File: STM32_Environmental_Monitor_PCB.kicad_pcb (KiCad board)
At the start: 2 copper layers, 90 x 81 mm, 29 parts, among them Q1 Q_NPN_EBC, Q2 Q_NPN_EBC, Q3 Q_NPN_EBC, Q4 Q_NPN_EBC, SW1 SW_Push, U1 NUCLEO-F303K8, U2 BME280-Module, U3 CC56-12SURKWA, U4 74HC595, U5 74HC595

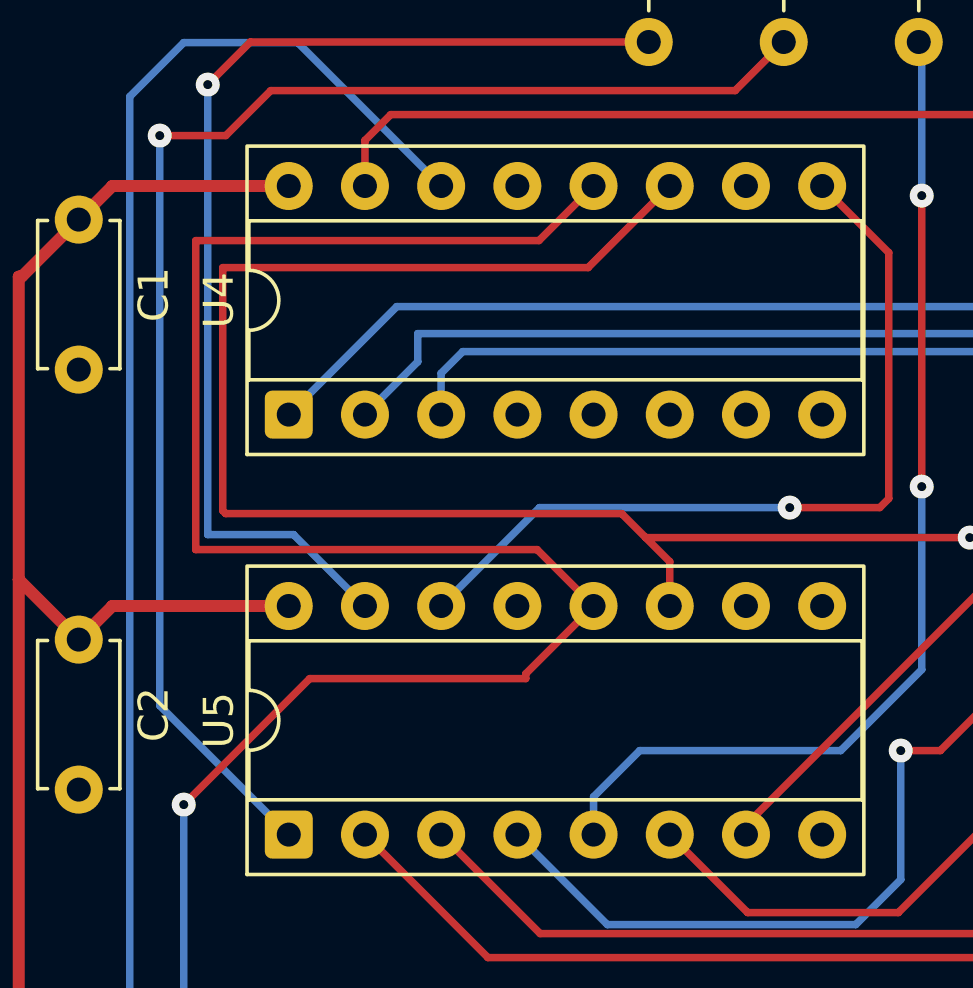
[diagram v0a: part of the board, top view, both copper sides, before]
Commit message: Fix 74HC595 control pins and update PCB fabrication files
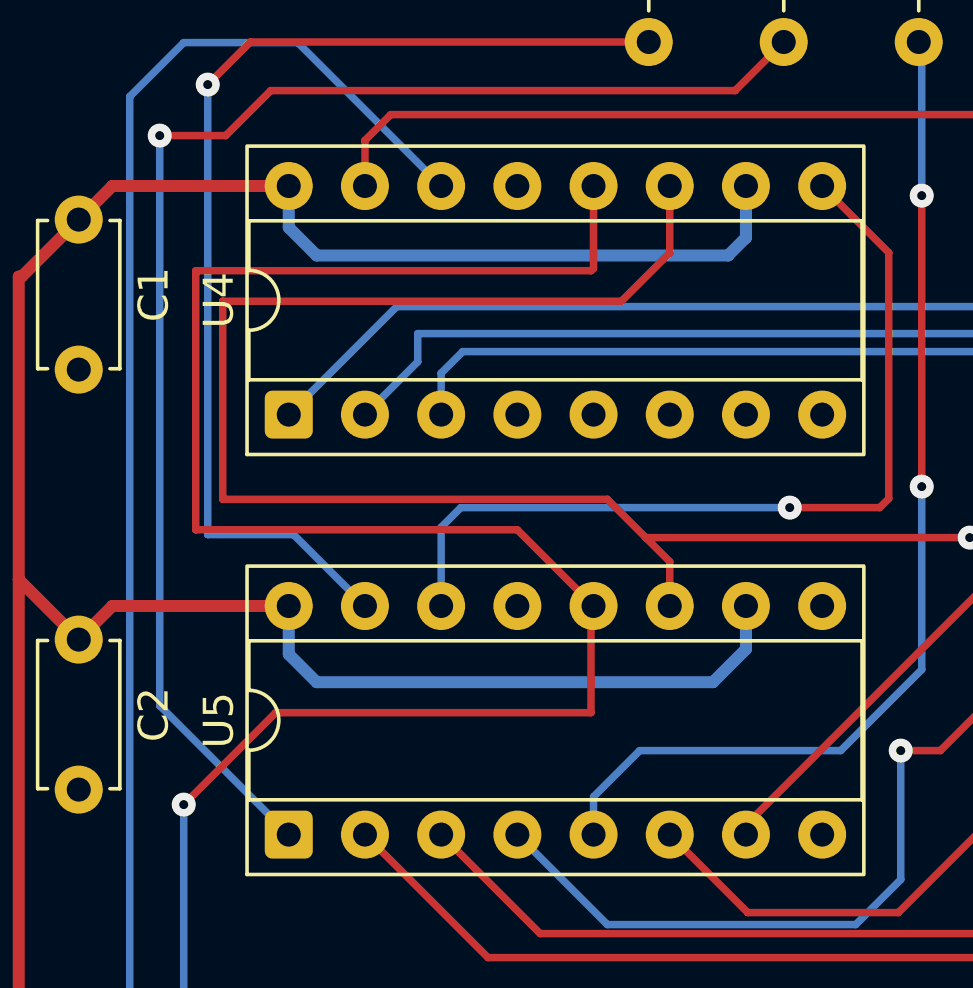
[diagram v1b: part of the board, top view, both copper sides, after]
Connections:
- U4 pad 10: unconnected-(U4-~{SRCLR}-Pad10) -> +3.3V
- U4 pad 13: unconnected-(U4-~{OE}-Pad13) -> GND
- U5 pad 10: unconnected-(U5-~{SRCLR}-Pad10) -> +3.3V
- U5 pad 13: unconnected-(U5-~{OE}-Pad13) -> GND
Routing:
- net +3.3V: track 155.7 -> 193.8 mm
- net Net-(U1-D9): track 102.6 -> 105.2 mm
- net Net-(U4-QH'): track 27.7 -> 29.3 mm
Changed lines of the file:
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@@
 		(sheetname "/")
 		(sheetfile "STM32_Environmental_Monitor_PCB.kicad_sch")
+		(units
+			(unit
+				(name "A")
+				(pins "2" "3" "1")
+			)
+		)
 		(attr through_hole)
 		(duplicate_pad_numbers_are_jumpers no)
@@
 		(sheetname "/")
 		(sheetfile "STM32_Environmental_Monitor_PCB.kicad_sch")
+		(units
+			(unit
+				(name "A")
+				(pins "2" "3" "1")
+			)
+		)
 		(attr through_hole)
 		(duplicate_pad_numbers_are_jumpers no)
@@
 			(layers "*.Cu" "*.Mask")
 			(remove_unused_layers no)
-			(net "unconnected-(U5-~{SRCLR}-Pad10)")
+			(net "+3.3V")
 			(pinfunction "~{SRCLR}_10")
-			(pintype "input+no_connect")
+			(pintype "input")
 		)
 		(pad "11" thru_hole circle
@@
 			(layers "*.Cu" "*.Mask")
 			(remove_unused_layers no)
-			(net "unconnected-(U5-~{OE}-Pad13)")
+			(net "GND")
 			(pinfunction "~{OE}_13")
-			(pintype "input+no_connect")
+			(pintype "input")
 		)
 		(pad "14" thru_hole circle
@@
 			(layers "*.Cu" "*.Mask")
 			(remove_unused_layers no)
-			(net "unconnected-(U4-~{SRCLR}-Pad10)")
+			(net "+3.3V")
 			(pinfunction "~{SRCLR}_10")
-			(pintype "input+no_connect")
+			(pintype "input")
 		)
 		(pad "11" thru_hole circle
@@
 			(layers "*.Cu" "*.Mask")
 			(remove_unused_layers no)
-			(net "unconnected-(U4-~{OE}-Pad13)")
+			(net "GND")
 			(pinfunction "~{OE}_13")
-			(pintype "input+no_connect")
+			(pintype "input")
 		)
 		(pad "14" thru_hole circle
@@
 		(sheetname "/")
 		(sheetfile "STM32_Environmental_Monitor_PCB.kicad_sch")
+		(units
+			(unit
+				(name "A")
+				(pins "2" "3" "1")
+			)
+		)
 		(attr through_hole)
 		(duplicate_pad_numbers_are_jumpers no)
@@
 		(sheetname "/")
 		(sheetfile "STM32_Environmental_Monitor_PCB.kicad_sch")
+		(units
+			(unit
+				(name "A")
+				(pins "2" "3" "1")
+			)
+		)
 		(attr through_hole)
 		(duplicate_pad_numbers_are_jumpers no)
@@
 	)
 	(segment
+		(start 90.932 107.696)
+		(end 90 106.764)
+		(width 0.4)
+		(layer "B.Cu")
+		(net "+3.3V")
+	)
+	(segment
+		(start 105.24 120.82)
+		(end 105.24 119.38)
+		(width 0.4)
+		(layer "B.Cu")
+		(net "+3.3V")
+	)
+	(segment
+		(start 90 120.988)
+		(end 90.932 121.92)
+		(width 0.4)
+		(layer "B.Cu")
+		(net "+3.3V")
+	)
+	(segment
+		(start 90 106.764)
+		(end 90 105.38)
+		(width 0.4)
+		(layer "B.Cu")
+		(net "+3.3V")
+	)
+	(segment
 		(start 161.96 136.3)
 		(end 165.35 139.69)
@@
 	)
 	(segment
+		(start 104.14 121.92)
+		(end 105.24 120.82)
+		(width 0.4)
+		(layer "B.Cu")
+		(net "+3.3V")
+	)
+	(segment
+		(start 90 119.38)
+		(end 90 120.988)
+		(width 0.4)
+		(layer "B.Cu")
+		(net "+3.3V")
+	)
+	(segment
+		(start 90.932 121.92)
+		(end 104.14 121.92)
+		(width 0.4)
+		(layer "B.Cu")
+		(net "+3.3V")
+	)
+	(segment
 		(start 155.2 136.3)
 		(end 161.96 136.3)
@@
 	)
 	(segment
+		(start 105.24 105.38)
+		(end 105.24 107.104)
+		(width 0.4)
+		(layer "B.Cu")
+		(net "+3.3V")
+	)
+	(segment
 		(start 147.5 139.4)
 		(end 150.6 136.3)
@@
 	)
 	(segment
+		(start 104.648 107.696)
+		(end 90.932 107.696)
+		(width 0.4)
+		(layer "B.Cu")
+		(net "+3.3V")
+	)
+	(segment
+		(start 105.24 107.104)
+		(end 104.648 107.696)
+		(width 0.4)
+		(layer "B.Cu")
+		(net "+3.3V")
+	)
+	(segment
 		(start 102.4 142.3)
 		(end 128.4 142.3)
@@
 	)
 	(segment
-		(start 90.7 121.8)
-		(end 97.9 121.8)
+		(start 100.076 108.204)
+		(end 86.9 108.204)
 		(width 0.25)
 		(layer "F.Cu")
@@
 	)
 	(segment
-		(start 86.9 117.5)
-		(end 98.28 117.5)
+		(start 89.564 122.936)
+		(end 100.076 122.936)
 		(width 0.25)
 		(layer "F.Cu")
@@
 	)
 	(segment
-		(start 86.5 126)
-		(end 90.7 121.8)
+		(start 86.9 108.204)
+		(end 86.9 116.84)
 		(width 0.25)
 		(layer "F.Cu")
@@
 	)
 	(segment
-		(start 98.28 117.5)
+		(start 97.62 116.84)
 		(end 100.16 119.38)
 		(width 0.25)
@@
 	)
 	(segment
-		(start 97.9 121.8)
-		(end 97.9 121.64)
+		(start 100.16 105.38)
+		(end 100.16 108.12)
+		(width 0.25)
+		(layer "F.Cu")
+		(net "Net-(U1-D9)")
+	)
+	(segment
+		(start 100.16 108.12)
+		(end 100.076 108.204)
 		(width 0.25)
 		(layer "F.Cu")
@@
 	)
 	(segment
-		(start 97.9 121.64)
+		(start 100.076 119.464)
 		(end 100.16 119.38)
 		(width 0.25)
@@
 	)
 	(segment
-		(start 98.34 107.2)
-		(end 86.9 107.2)
+		(start 86.5 126)
+		(end 89.564 122.936)
 		(width 0.25)
 		(layer "F.Cu")
@@
 	)
 	(segment
-		(start 100.16 105.38)
-		(end 98.34 107.2)
+		(start 100.076 122.936)
+		(end 100.076 119.464)
 		(width 0.25)
 		(layer "F.Cu")
@@
 	)
 	(segment
-		(start 86.9 107.2)
-		(end 86.9 117.5)
+		(start 86.9 116.84)
+		(end 97.62 116.84)
 		(width 0.25)
 		(layer "F.Cu")
@@
 	)
 	(segment
-		(start 87.9 116.3)
-		(end 101.1 116.3)
+		(start 87.8 115.824)
+		(end 100.624 115.824)
 		(width 0.25)
 		(layer "F.Cu")
@@
 	)
 	(segment
-		(start 99.98 108.1)
-		(end 87.8 108.1)
+		(start 101.092 109.22)
+		(end 87.8 109.22)
 		(width 0.25)
 		(layer "F.Cu")
@@
 	)
 	(segment
-		(start 87.8 116.2)
-		(end 87.9 116.3)
+		(start 102.7 107.612)
+		(end 101.092 109.22)
 		(width 0.25)
 		(layer "F.Cu")
@@
 	)
 	(segment
-		(start 87.8 108.1)
-		(end 87.8 116.2)
+		(start 87.8 109.22)
+		(end 87.8 115.824)
 		(width 0.25)
 		(layer "F.Cu")
@@
 	)
 	(segment
-		(start 102.7 117.9)
-		(end 102.7 119.38)
+		(start 100.624 115.824)
+		(end 101.9 117.1)
 		(width 0.25)
 		(layer "F.Cu")
@@
 	)
 	(segment
-		(start 112.7 117.1)
-		(end 101.9 117.1)
+		(start 102.7 117.9)
+		(end 102.7 119.38)
 		(width 0.25)
 		(layer "F.Cu")
@@
 	)
 	(segment
-		(start 101.1 116.3)
+		(start 112.7 117.1)
 		(end 101.9 117.1)
 		(width 0.25)
@@
 	)
 	(segment
-		(start 102.7 105.38)
-		(end 99.98 108.1)
+		(start 101.9 117.1)
+		(end 102.7 117.9)
 		(width 0.25)
 		(layer "F.Cu")
@@
 	)
 	(segment
-		(start 101.9 117.1)
-		(end 102.7 117.9)
+		(start 102.7 105.38)
+		(end 102.7 107.612)
 		(width 0.25)
 		(layer "F.Cu")
@@
 	)
 	(segment
+		(start 95.08 116.756)
+		(end 95.08 119.38)
+		(width 0.25)
+		(layer "B.Cu")
+		(net "Net-(U4-QH')")
+	)
+	(segment
 		(start 106.7 116.1)
-		(end 98.36 116.1)
+		(end 95.736 116.1)
 		(width 0.25)
 		(layer "B.Cu")
@@
 	)
 	(segment
-		(start 98.36 116.1)
-		(end 95.08 119.38)
+		(start 95.736 116.1)
+		(end 95.08 116.756)
 		(width 0.25)
 		(layer "B.Cu")
